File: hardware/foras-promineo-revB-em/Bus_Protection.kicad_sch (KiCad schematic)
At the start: 53 parts, among them Q11 MMDT2907AQ-7-F, Q12 BSS138DWQ-7, Q13 BSS138DWQ-7, Q15 MMDT5551-7-F, Q16 MMDT5551-7-F, Q17 FJV992FMTF, Q18 BSS138DWQ-7, Q19 BSS138DWQ-7, Q7 MMDT5551-7-F, Q8 MMDT5551-7-F

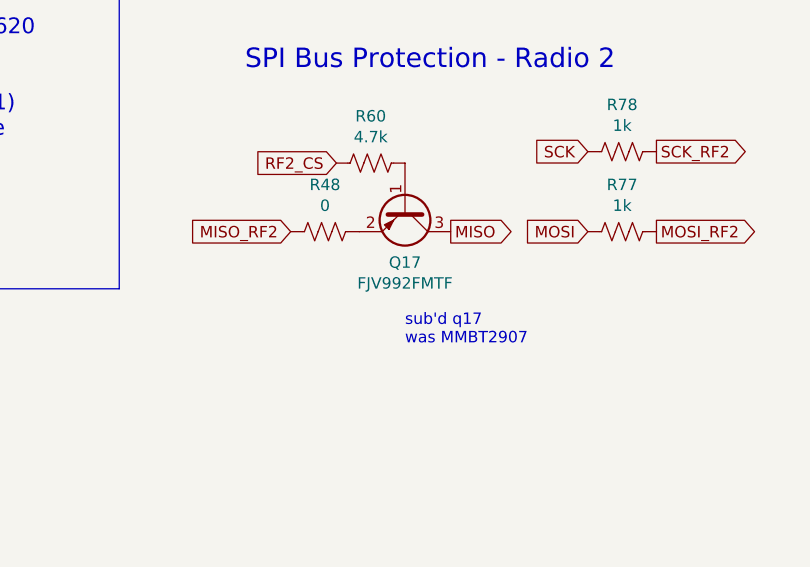
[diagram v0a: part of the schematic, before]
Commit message: updated em board for pcbway 6-layer tu-862 fabrication
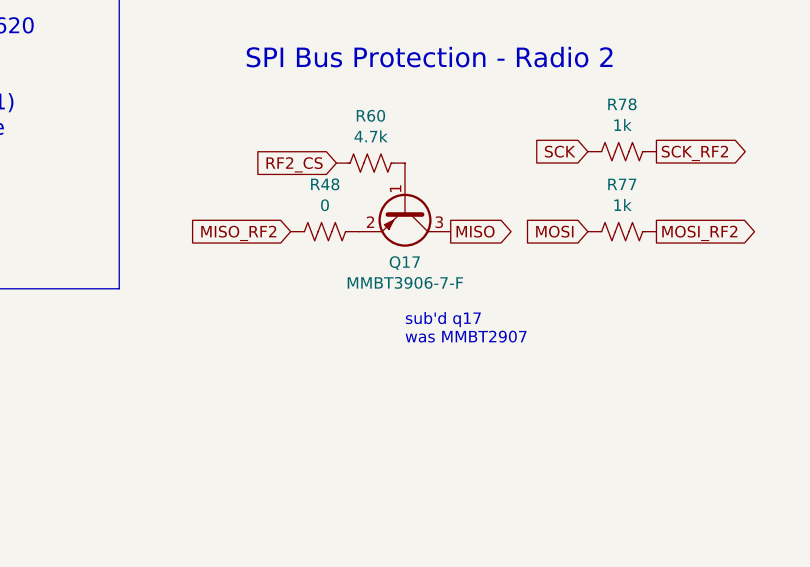
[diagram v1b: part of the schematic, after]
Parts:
- Q17: value FJV992FMTF -> MMBT3906-7-F
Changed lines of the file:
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@@
     (in_bom yes) (on_board yes)
     (property "Reference" "Q17" (id 0) (at 213.36 116.459 90))
-    (property "Value" "FJV992FMTF" (id 1) (at 213.36 118.7704 90))
+    (property "Value" "MMBT3906-7-F" (id 1) (at 213.36 118.7704 90))
     (property "Footprint" "Package_TO_SOT_SMD:SOT-23" (id 2) (at 211.455 115.57 0)
       (effects (font (size 1.27 1.27) italic) (justify left) hide)
